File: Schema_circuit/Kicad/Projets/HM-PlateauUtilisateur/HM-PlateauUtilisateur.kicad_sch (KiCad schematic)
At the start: 16 parts, among them J1A Vient de la base, J2 Conn_01x12_Socket, J3 Conn_01x12_Socket, J3A Extension touches, J4 Conn_01x02_Pin, J5A Afficheur, J5B Conn_01x04_Pin, J6 5A/5B, J7 5C/5D, J8 Conn_01x02_Socket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

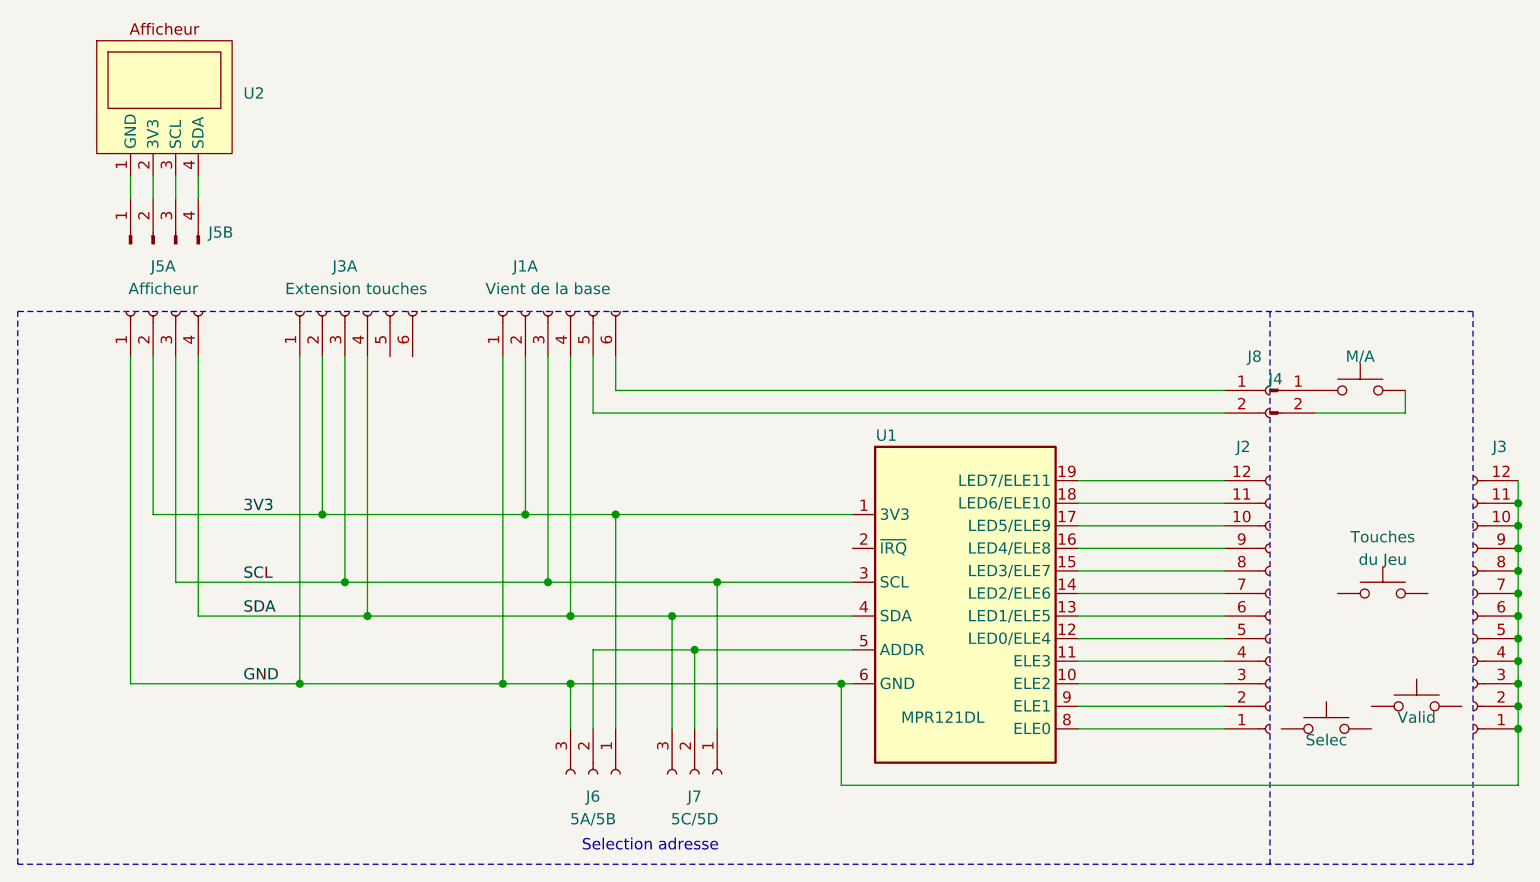
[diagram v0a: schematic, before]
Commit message: correctif sur PCB PU1
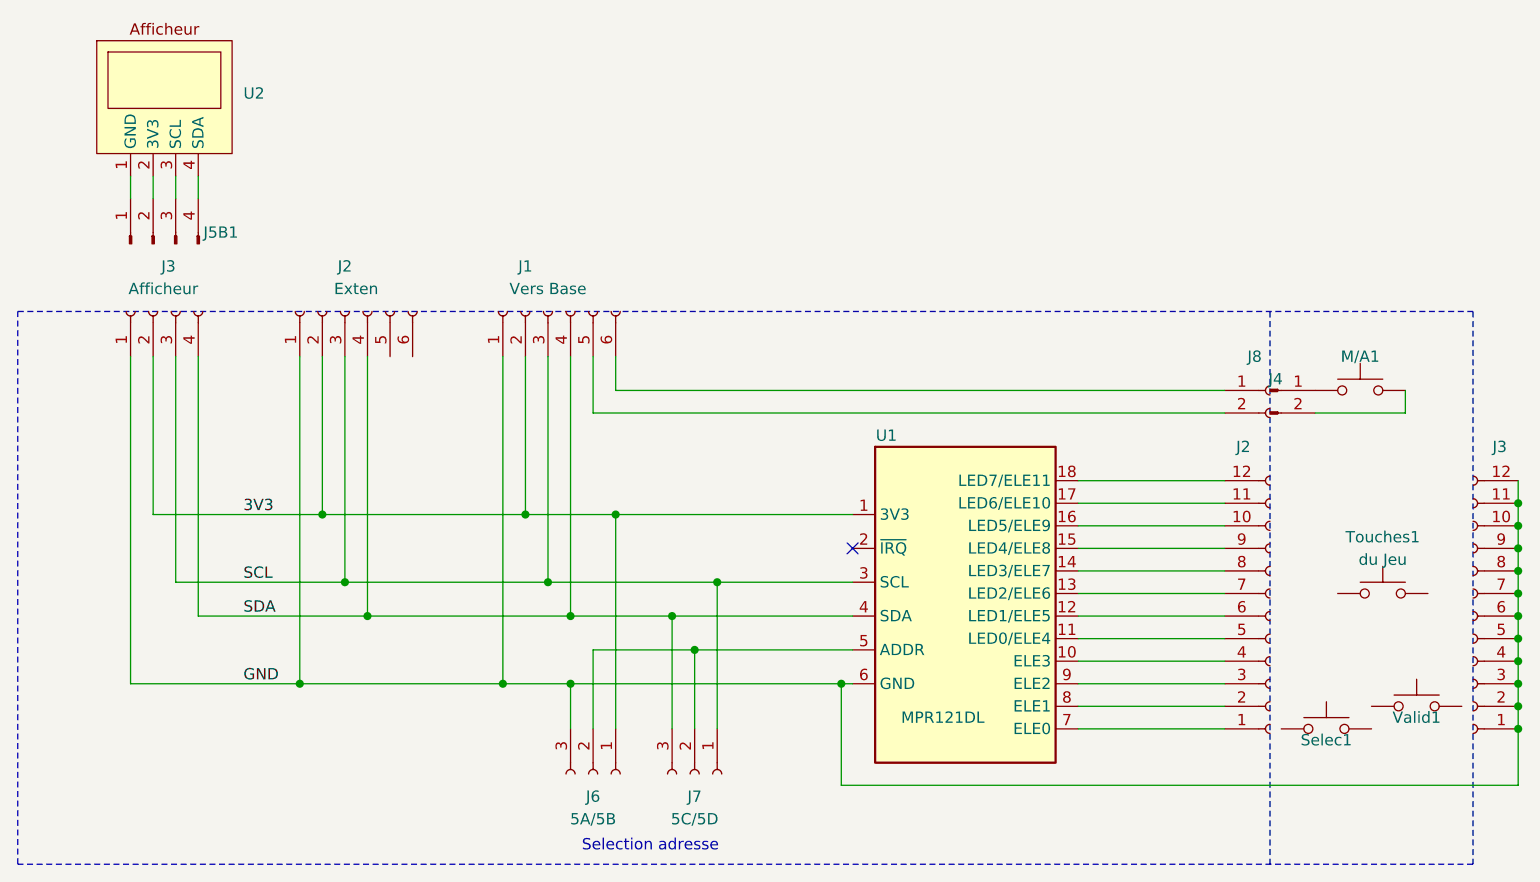
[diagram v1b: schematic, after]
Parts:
- J1: renamed from J1A; value Vient de la base -> Vers Base; footprint (none) -> MesEmpreintes2:SIP-6
- J2, J3: footprint (none) -> MesEmpreintes2:SIP-12
- J2: renamed from J3A; value Extension touches -> Exten; footprint (none) -> MesEmpreintes2:SIP-6
- J3: renamed from J5A; footprint (none) -> MesEmpreintes2:SIP-4
- J6, J7: footprint (none) -> MesEmpreintes2:SIP-3
- J8: footprint (none) -> MesEmpreintes2:SIP-2
- renumbered J5B to J5B1, M/A to M/A1, Selec to Selec1, Touches to Touches1, Valid to Valid1
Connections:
- net at J2.1 (Pin_1): now also U1.7 (ELE0); no longer U1.8 (ELE0)
- net at J2.10 (Pin_10): now also U1.16 (LED5/ELE9); no longer U1.17 (LED5/ELE9)
- net at J2.11 (Pin_11): now also U1.17 (LED6/ELE10); no longer U1.18 (LED6/ELE10)
- net at J2.12 (Pin_12): now also U1.18 (LED7/ELE11); no longer U1.19 (LED7/ELE11)
- net at J2.2 (Pin_2): now also U1.8 (ELE1); no longer U1.9 (ELE1)
- net at J2.3 (Pin_3): now also U1.9 (ELE2); no longer U1.10 (ELE2)
- net at J2.4 (Pin_4): now also U1.10 (ELE3); no longer U1.11 (ELE3)
- net at J2.5 (Pin_5): now also U1.11 (LED0/ELE4); no longer U1.12 (LED0/ELE4)
- net at J2.6 (Pin_6): now also U1.12 (LED1/ELE5); no longer U1.13 (LED1/ELE5)
- net at J2.7 (Pin_7): now also U1.13 (LED2/ELE6); no longer U1.14 (LED2/ELE6)
- net at J2.8 (Pin_8): now also U1.14 (LED3/ELE7); no longer U1.15 (LED3/ELE7)
- net at J2.9 (Pin_9): now also U1.15 (LED4/ELE8); no longer U1.16 (LED4/ELE8)
- no-connect marks 0 -> 1
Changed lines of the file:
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@@
   (junction (at 229.87 97.79) (diameter 0) (color 0 0 0 0)
   )
+  (no_connect (at 154.94 100.33))
   (wire (pts (xy 81.28 78.74) (xy 81.28 107.95))
     (stroke (width 0) (type default))
@@
   (symbol (lib_id "Connector:Conn_01x04_Socket") (at 76.2 73.66 90) (unit 1)
     (in_bom yes) (on_board yes) (dnp no)
-    (property "Reference" "J5A" (at 78.74 68.58 90)
+    (property "Reference" "J3" (at 78.74 68.58 90)
       (effects (font (size 1.27 1.27)) (justify left))
     )
@@
       (effects (font (size 1.27 1.27)) (justify left))
     )
-    (property "Footprint" "" (at 76.2 73.66 0)
+    (property "Footprint" "MesEmpreintes2:SIP-4" (at 76.2 73.66 0)
       (effects (font (size 1.27 1.27)) hide)
     )
@@
       (project "HM-PlateauUtilisateur"
         (path "/85751984-1fbc-4360-b0b3-a85f996736e6"
-          (reference "J5A") (unit 1)
+          (reference "J3") (unit 1)
         )
       )
@@
       (effects (font (size 1.27 1.27)))
     )
-    (property "Footprint" "" (at 125.73 125.73 0)
+    (property "Footprint" "MesEmpreintes2:SIP-3" (at 125.73 125.73 0)
       (effects (font (size 1.27 1.27)) hide)
     )
@@
   (symbol (lib_id "Connector:Conn_01x04_Pin") (at 76.2 66.04 90) (unit 1)
     (in_bom yes) (on_board no) (dnp no)
-    (property "Reference" "J5B" (at 83.82 64.77 90)
+    (property "Reference" "J5B1" (at 83.82 64.77 90)
       (effects (font (size 1.27 1.27)))
     )
@@
       (project "HM-PlateauUtilisateur"
         (path "/85751984-1fbc-4360-b0b3-a85f996736e6"
-          (reference "J5B") (unit 1)
+          (reference "J5B1") (unit 1)
         )
       )
@@
   (symbol (lib_id "Switch:SW_Push") (at 218.44 118.11 0) (unit 1)
     (in_bom yes) (on_board no) (dnp no)
-    (property "Reference" "Valid" (at 218.44 119.38 0)
+    (property "Reference" "Valid1" (at 218.44 119.38 0)
       (effects (font (size 1.27 1.27)))
     )
@@
       (project "HM-PlateauUtilisateur"
         (path "/85751984-1fbc-4360-b0b3-a85f996736e6"
-          (reference "Valid") (unit 1)
+          (reference "Valid1") (unit 1)
         )
       )
@@
       (effects (font (size 1.27 1.27)))
     )
-    (property "Footprint" "" (at 137.16 125.73 0)
+    (property "Footprint" "MesEmpreintes2:SIP-3" (at 137.16 125.73 0)
       (effects (font (size 1.27 1.27)) hide)
     )
@@
       (effects (font (size 1.27 1.27)) (justify left) hide)
     )
-    (property "Footprint" "" (at 201.93 107.95 0)
+    (property "Footprint" "MesEmpreintes2:SIP-12" (at 201.93 107.95 0)
       (effects (font (size 1.27 1.27)) hide)
     )
@@
   (symbol (lib_id "Switch:SW_Push") (at 208.28 120.65 0) (unit 1)
     (in_bom yes) (on_board no) (dnp no)
-    (property "Reference" "Selec" (at 208.28 121.92 0)
+    (property "Reference" "Selec1" (at 208.28 121.92 0)
       (effects (font (size 1.27 1.27)))
     )
@@
       (project "HM-PlateauUtilisateur"
         (path "/85751984-1fbc-4360-b0b3-a85f996736e6"
-          (reference "Selec") (unit 1)
+          (reference "Selec1") (unit 1)
         )
       )
@@
       (effects (font (size 1.27 1.27)) (justify left) hide)
     )
-    (property "Footprint" "" (at 201.93 82.55 0)
+    (property "Footprint" "MesEmpreintes2:SIP-2" (at 201.93 82.55 0)
       (effects (font (size 1.27 1.27)) hide)
     )
@@
       (effects (font (size 1.27 1.27)) (justify left) hide)
     )
-    (property "Footprint" "" (at 224.79 107.95 0)
+    (property "Footprint" "MesEmpreintes2:SIP-12" (at 224.79 107.95 0)
       (effects (font (size 1.27 1.27)) hide)
     )
@@
   (symbol (lib_id "Switch:SW_Push") (at 212.09 82.55 0) (unit 1)
     (in_bom yes) (on_board no) (dnp no)
-    (property "Reference" "M/A" (at 212.09 78.74 0)
+    (property "Reference" "M/A1" (at 212.09 78.74 0)
       (effects (font (size 1.27 1.27)))
     )
@@
       (project "HM-PlateauUtilisateur"
         (path "/85751984-1fbc-4360-b0b3-a85f996736e6"
-          (reference "M/A") (unit 1)
+          (reference "M/A1") (unit 1)
         )
       )
@@
   (symbol (lib_id "Connector:Conn_01x06_Socket") (at 120.65 73.66 90) (unit 1)
     (in_bom yes) (on_board yes) (dnp no)
-    (property "Reference" "J1A" (at 118.11 68.58 90)
-      (effects (font (size 1.27 1.27)))
-    )
-    (property "Value" "Vient de la base" (at 120.65 71.12 90)
-      (effects (font (size 1.27 1.27)))
-    )
-    (property "Footprint" "" (at 120.65 73.66 0)
+    (property "Reference" "J1" (at 118.11 68.58 90)
+      (effects (font (size 1.27 1.27)))
+    )
+    (property "Value" "Vers Base" (at 120.65 71.12 90)
+      (effects (font (size 1.27 1.27)))
+    )
+    (property "Footprint" "MesEmpreintes2:SIP-6" (at 120.65 73.66 0)
       (effects (font (size 1.27 1.27)) hide)
     )
@@
       (project "HM-PlateauUtilisateur"
         (path "/85751984-1fbc-4360-b0b3-a85f996736e6"
-          (reference "J1A") (unit 1)
+          (reference "J1") (unit 1)
         )
       )
@@
     (pin "17")
     (pin "18")
-    (pin "19")
     (pin "2")
     (pin "3")
@@
     (pin "5")
     (pin "6")
+    (pin "7")
     (pin "8")
     (pin "9")
@@
   (symbol (lib_id "Switch:SW_Push") (at 214.63 105.41 0) (unit 1)
     (in_bom yes) (on_board no) (dnp no)
-    (property "Reference" "Touches" (at 214.63 99.06 0)
+    (property "Reference" "Touches1" (at 214.63 99.06 0)
       (effects (font (size 1.27 1.27)))
     )
@@
       (project "HM-PlateauUtilisateur"
         (path "/85751984-1fbc-4360-b0b3-a85f996736e6"
-          (reference "Touches") (unit 1)
+          (reference "Touches1") (unit 1)
         )
       )
@@
   (symbol (lib_id "Connector:Conn_01x06_Socket") (at 97.79 73.66 90) (unit 1)
     (in_bom yes) (on_board yes) (dnp no)
-    (property "Reference" "J3A" (at 97.79 68.58 90)
-      (effects (font (size 1.27 1.27)))
-    )
-    (property "Value" "Extension touches" (at 99.06 71.12 90)
-      (effects (font (size 1.27 1.27)))
-    )
-    (property "Footprint" "" (at 97.79 73.66 0)
+    (property "Reference" "J2" (at 97.79 68.58 90)
+      (effects (font (size 1.27 1.27)))
+    )
+    (property "Value" "Exten" (at 99.06 71.12 90)
+      (effects (font (size 1.27 1.27)))
+    )
+    (property "Footprint" "MesEmpreintes2:SIP-6" (at 97.79 73.66 0)
       (effects (font (size 1.27 1.27)) hide)
     )
@@
       (project "HM-PlateauUtilisateur"
         (path "/85751984-1fbc-4360-b0b3-a85f996736e6"
-          (reference "J3A") (unit 1)
-        )
-      )
+          (reference "J2") (unit 1)
+        )
+      )
